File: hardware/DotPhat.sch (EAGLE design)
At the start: 41 parts, among them CN1 1X4-BIG, IC1 CAT24M010TS, J2 RASPBERRYPI-40-PIN-GPIO_PTH, J3 USB-MICROB, U1 ATMEGA328P-MU-QFN32, U2 TMP102, U3 ATSHA204-TSU, X3 S4B-ZR

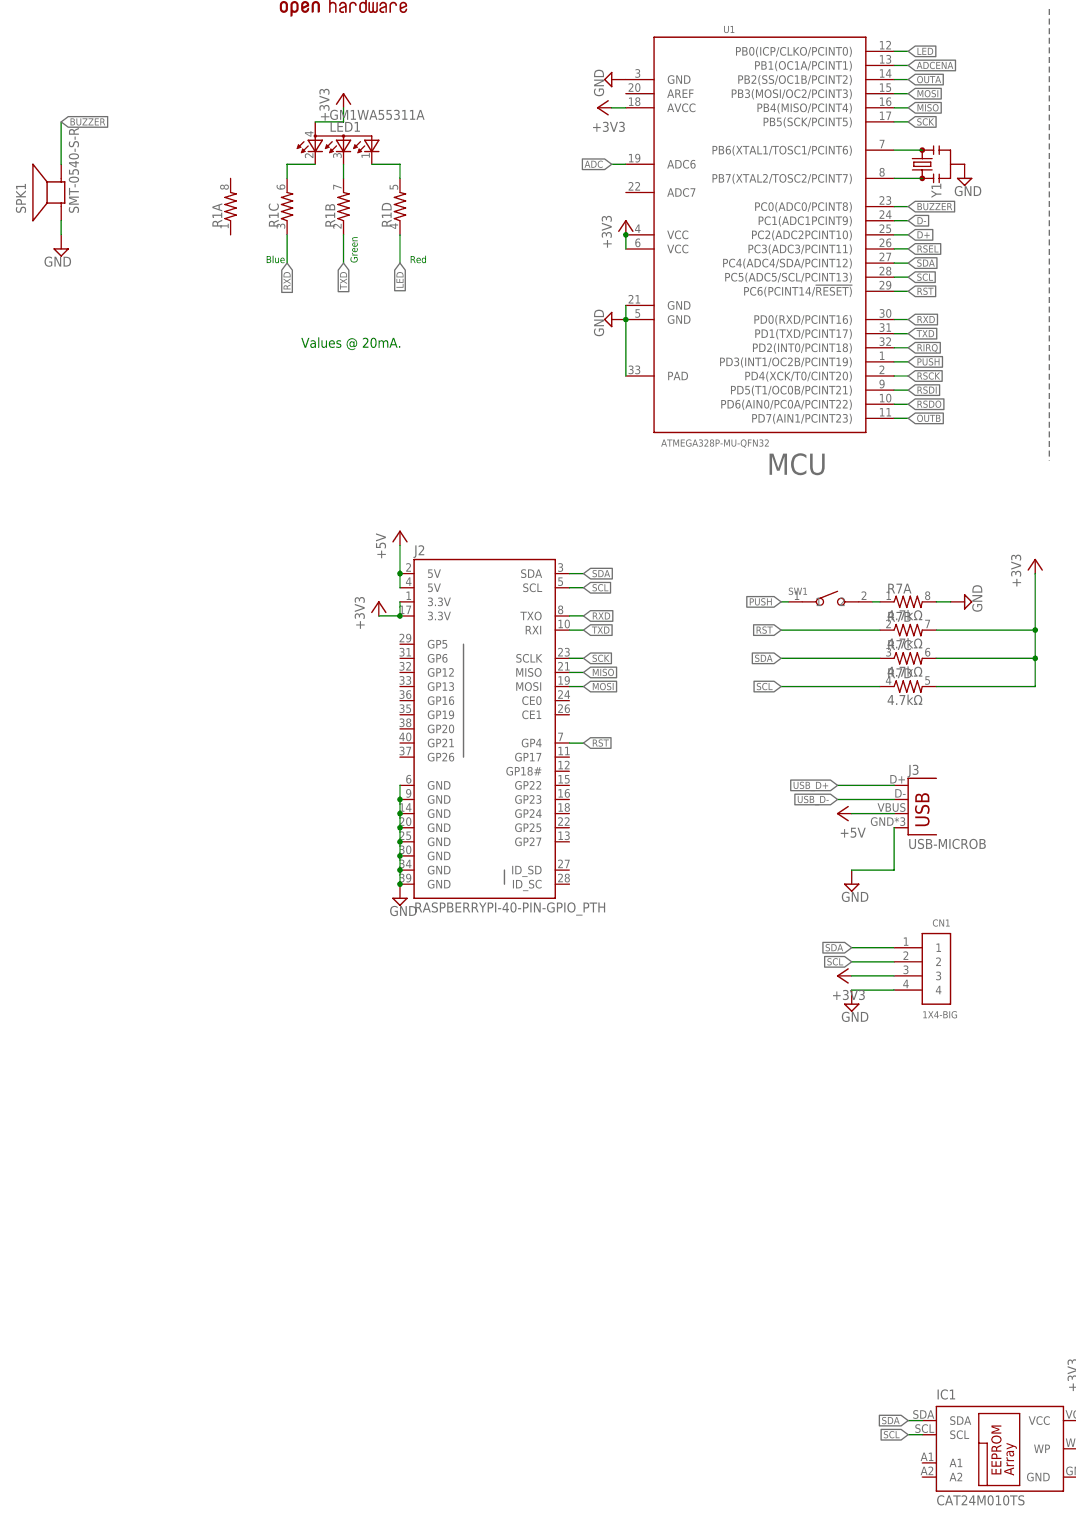
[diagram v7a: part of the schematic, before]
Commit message: Add 128Mbit SPI Flash
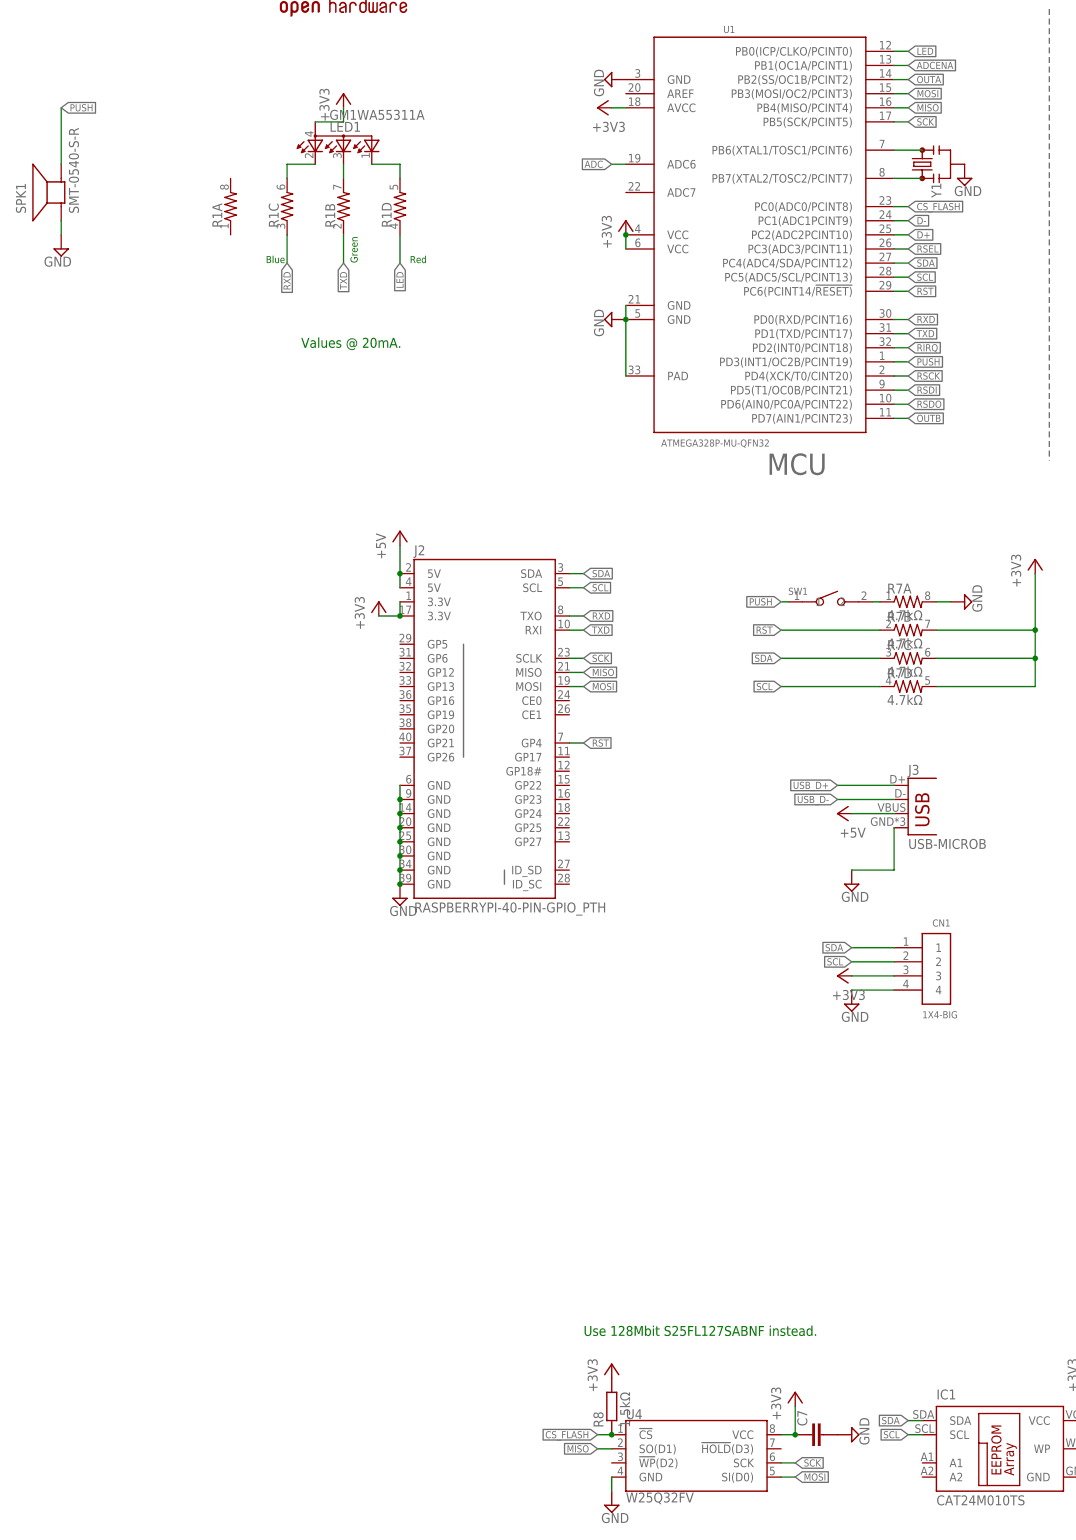
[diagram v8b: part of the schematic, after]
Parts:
- added C7: (no value), rcl:C-EUC0603
- added R8: 1.5kΩ, rcl:R-EU_R0603
- added U4: W25Q32FV, SparkFun-IC-Memory:W25Q32FVZP
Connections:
- removed net BUZZER: SPK1.-, U1.PC0(ADC0/PCINT8)
- new net CS_FLASH: R8.1, U1.PC0(ADC0/PCINT8), U4.!CS!
- net +3V3: now also C7.1, R8.2, U4.VCC
- net GND: now also C7.2, U4.GND
- net MISO: now also U4.SO(D1)
- net MOSI: now also U4.SI(D0)
- net PUSH: now also SPK1.-
- net SCK: now also U4.SCK
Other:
- note added: "Use 128Mbit S25FL127SABNF instead."
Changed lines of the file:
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@@
 <part name="JP4" library="SparkFun-Jumpers" deviceset="JUMPER-SMT_2_NC_TRACE" device="_NO-SILK"/>
 <part name="+3V16" library="supply1" deviceset="+3V3" device=""/>
+<part name="U4" library="SparkFun-IC-Memory" deviceset="W25Q32FV" device="ZP" value="W25Q32FV"/>
+<part name="+3V17" library="supply1" deviceset="+3V3" device=""/>
+<part name="SUPPLY23" library="supply2" deviceset="GND" device=""/>
+<part name="SUPPLY24" library="supply2" deviceset="GND" device=""/>
+<part name="C7" library="rcl" deviceset="C-EU" device="C0603"/>
+<part name="R8" library="rcl" deviceset="R-EU_" device="R0603" value="1.5kΩ"/>
+<part name="+3V18" library="supply1" deviceset="+3V3" device=""/>
 </parts>
 <sheets>
@@
 <text x="134.62" y="134.62" size="1.778" layer="91">white</text>
 <text x="134.62" y="124.46" size="1.778" layer="91">red</text>
+<text x="20.32" y="-142.24" size="1.778" layer="91">Use 128Mbit S25FL127SABNF instead.</text>
 </plain>
 <instances>
@@
 <instance part="JP4" gate="G$1" x="231.14" y="81.28"/>
 <instance part="+3V16" gate="G$1" x="254" y="-38.1"/>
+<instance part="U4" gate="G$1" x="40.64" y="-162.56"/>
+<instance part="+3V17" gate="G$1" x="58.42" y="-152.4"/>
+<instance part="SUPPLY23" gate="GND" x="25.4" y="-172.72"/>
+<instance part="SUPPLY24" gate="GND" x="68.58" y="-160.02" rot="R90"/>
+<instance part="C7" gate="G$1" x="60.96" y="-160.02" rot="R90"/>
+<instance part="R8" gate="G$1" x="25.4" y="-154.94" rot="R90"/>
+<instance part="+3V18" gate="G$1" x="25.4" y="-147.32"/>
 </instances>
 <busses>
@@
 <pinref part="SUPPLY22" gate="GND" pin="GND"/>
 </segment>
+<segment>
+<pinref part="U4" gate="G$1" pin="GND"/>
+<pinref part="SUPPLY23" gate="GND" pin="GND"/>
+<wire x1="25.4" y1="-167.64" x2="25.4" y2="-170.18" width="0.1524" layer="91"/>
+</segment>
+<segment>
+<pinref part="SUPPLY24" gate="GND" pin="GND"/>
+<pinref part="C7" gate="G$1" pin="2"/>
+</segment>
 </net>
 <net name="SDA" class="0">
@@
 <pinref part="+3V16" gate="G$1" pin="+3V3"/>
 </segment>
+<segment>
+<pinref part="U4" gate="G$1" pin="VCC"/>
+<pinref part="+3V17" gate="G$1" pin="+3V3"/>
+<wire x1="55.88" y1="-160.02" x2="58.42" y2="-160.02" width="0.1524" layer="91"/>
+<wire x1="58.42" y1="-160.02" x2="58.42" y2="-154.94" width="0.1524" layer="91"/>
+<pinref part="C7" gate="G$1" pin="1"/>
+<junction x="58.42" y="-160.02"/>
+</segment>
+<segment>
+<pinref part="R8" gate="G$1" pin="2"/>
+<pinref part="+3V18" gate="G$1" pin="+3V3"/>
+</segment>
 </net>
 <net name="ADCENA" class="0">
@@
 <label x="52.07" y="125.73" size="1.27" layer="95" rot="R180" xref="yes"/>
 </segment>
+<segment>
+<pinref part="U4" gate="G$1" pin="SI(D0)"/>
+<wire x1="55.88" y1="-167.64" x2="58.42" y2="-167.64" width="0.1524" layer="91"/>
+<label x="58.42" y="-167.64" size="1.27" layer="95" xref="yes"/>
+</segment>
 </net>
 <net name="MISO" class="0">
@@
 <label x="52.07" y="123.19" size="1.27" layer="95" rot="R180" xref="yes"/>
 </segment>
+<segment>
+<pinref part="U4" gate="G$1" pin="SO(D1)"/>
+<wire x1="25.4" y1="-162.56" x2="22.86" y2="-162.56" width="0.1524" layer="91"/>
+<label x="22.86" y="-162.56" size="1.27" layer="95" rot="R180" xref="yes"/>
+</segment>
 </net>
 <net name="TXD" class="0">
@@
 <label x="52.07" y="120.65" size="1.27" layer="95" rot="R180" xref="yes"/>
 </segment>
+<segment>
+<pinref part="U4" gate="G$1" pin="SCK"/>
+<wire x1="55.88" y1="-165.1" x2="58.42" y2="-165.1" width="0.1524" layer="91"/>
+<label x="58.42" y="-165.1" size="1.27" layer="95" xref="yes"/>
+</segment>
 </net>
 <net name="SCL" class="0">
@@
 <wire x1="57.15" y1="-10.16" x2="55.88" y2="-10.16" width="0.1524" layer="91"/>
 <label x="55.88" y="-10.16" size="1.27" layer="95" rot="R180" xref="yes"/>
+</segment>
+<segment>
+<pinref part="SPK1" gate="G$1" pin="-"/>
+<wire x1="-73.66" y1="68.58" x2="-73.66" y2="78.74" width="0.1524" layer="91"/>
+<label x="-73.66" y="78.74" size="1.27" layer="95" xref="yes"/>
 </segment>
 </net>
@@
 <wire x1="27.94" y1="68.58" x2="25.4" y2="68.58" width="0.1524" layer="91"/>
 <label x="25.4" y="68.58" size="1.27" layer="95" rot="R180" xref="yes"/>
-</segment>
-</net>
-<net name="BUZZER" class="0">
-<segment>
-<pinref part="U1" gate="G$1" pin="PC0(ADC0/PCINT8)"/>
-<wire x1="76.2" y1="60.96" x2="78.74" y2="60.96" width="0.1524" layer="91"/>
-<label x="78.74" y="60.96" size="1.27" layer="95" xref="yes"/>
-</segment>
-<segment>
-<pinref part="SPK1" gate="G$1" pin="-"/>
-<wire x1="-73.66" y1="68.58" x2="-73.66" y2="76.2" width="0.1524" layer="91"/>
-<label x="-73.66" y="76.2" size="1.27" layer="95" xref="yes"/>
 </segment>
 </net>
@@
 </segment>
 </net>
+<net name="CS_FLASH" class="0">
+<segment>
+<pinref part="U4" gate="G$1" pin="!CS!"/>
+<pinref part="R8" gate="G$1" pin="1"/>
+<wire x1="25.4" y1="-160.02" x2="22.86" y2="-160.02" width="0.1524" layer="91"/>
+<junction x="25.4" y="-160.02"/>
+<label x="22.86" y="-160.02" size="1.27" layer="95" rot="R180" xref="yes"/>
+</segment>
+<segment>
+<pinref part="U1" gate="G$1" pin="PC0(ADC0/PCINT8)"/>
+<wire x1="76.2" y1="60.96" x2="78.74" y2="60.96" width="0.1524" layer="91"/>
+<label x="78.74" y="60.96" size="1.27" layer="95" xref="yes"/>
+</segment>
+</net>
